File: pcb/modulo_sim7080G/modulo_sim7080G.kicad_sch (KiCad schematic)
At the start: 9 parts, among them J1 Conn_01x02, J2 Conn_01x02, J3 Conn_01x07, U1 SIM7080G, U2 TXB0108DQSR

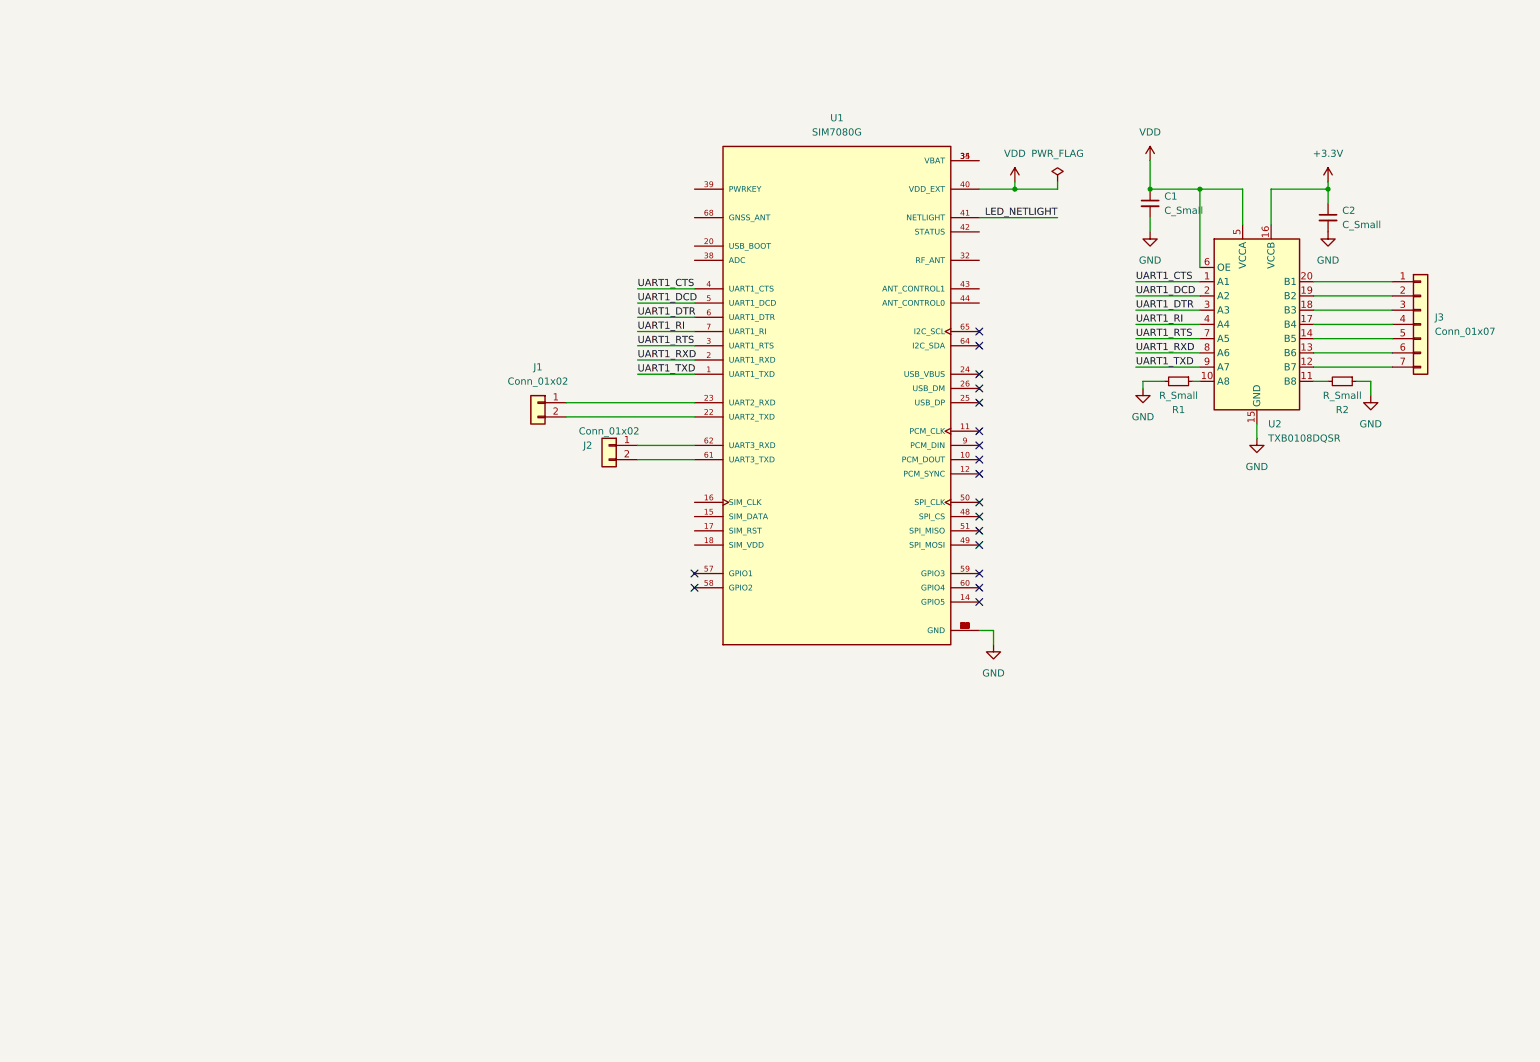
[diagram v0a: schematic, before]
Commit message: update schematic
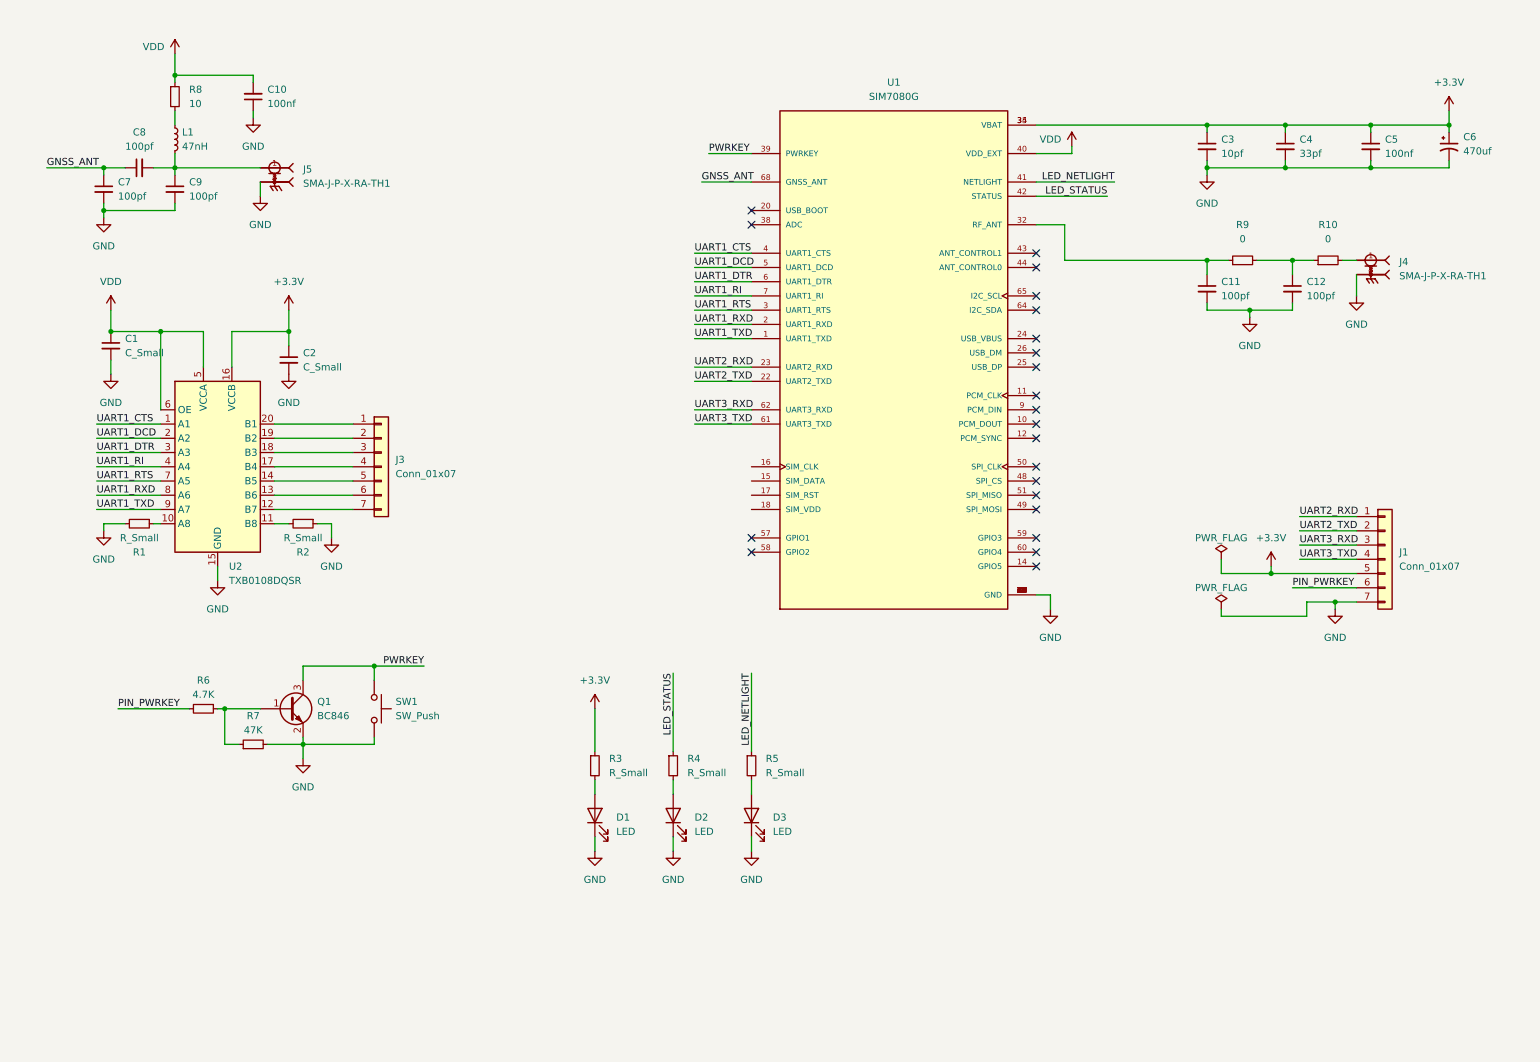
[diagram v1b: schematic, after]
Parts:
- removed J1, J2: Conn_01x02, Connector_PinHeader_2.54mm:PinHeader_1x02_P2.54mm_Vertical, symbol Connector_Generic:Conn_01x02
- added C10, C5: 100nf, Capacitor_SMD:C_0805_2012Metric, symbol Device:C_Small
- added C11, C12, C7, C8, C9: 100pf, Capacitor_SMD:C_0805_2012Metric, symbol Device:C_Small
- added C3: 10pf, Capacitor_SMD:C_0805_2012Metric, symbol Device:C_Small
- added C4: 33pf, Capacitor_SMD:C_0805_2012Metric, symbol Device:C_Small
- added C6: 470uf, Capacitor_Tantalum_SMD:CP_EIA-2012-12_Kemet-R, symbol Device:C_Polarized_Small_US
- added D1, D2, D3: LED, LED_SMD:LED_0805_2012Metric, symbol Device:LED
- added J1: Conn_01x07, Connector_PinHeader_2.54mm:PinHeader_1x07_P2.54mm_Vertical, symbol Connector_Generic:Conn_01x07
- added J4, J5: SMA-J-P-X-RA-TH1, SMA-J-P-X-RA-TH1:SAMTEC_SMA-J-P-X-RA-TH1, symbol SMA-J-P-X-RA-TH1:SMA-J-P-X-RA-TH1
- added L1: 47nH, Inductor_SMD:L_0805_2012Metric, symbol Device:L_Small
- added Q1: BC846, Package_TO_SOT_SMD:SOT-23, symbol Transistor_BJT:BC846
- added R10, R9: 0, Resistor_SMD:R_0805_2012Metric, symbol Device:R_Small
- added R3, R4, R5: R_Small, Resistor_SMD:R_0805_2012Metric, symbol Device:R_Small
- added R6: 4.7K, Resistor_SMD:R_0805_2012Metric, symbol Device:R_Small
- added R7: 47K, Resistor_SMD:R_0805_2012Metric, symbol Device:R_Small
- added R8: 10, Resistor_SMD:R_0805_2012Metric, symbol Device:R_Small
- added SW1: SW_Push, Button_Switch_SMD:SW_SPST_B3U-1000P-B, symbol Switch:SW_Push
- C1, C2: footprint (none) -> Capacitor_SMD:C_0805_2012Metric
- R1, R2: footprint (none) -> Resistor_SMD:R_0805_2012Metric
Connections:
- net +3.3V: now also U1.34 (VBAT), U1.35 (VBAT), C3.1, C4.1, C5.1, C6.1, J1.5 (Pin_5), R3.1
- net GND: now also C10.1, C11.2, C12.2, C3.2, C4.2, C5.2, C6.2, C7.2, C9.2, D1.1 (K), D2.1 (K), D3.1 (K), J1.7 (Pin_7), J4.2, J4.3, J4.4, J4.5, J5.2, J5.3, J5.4, J5.5, Q1.2 (E), R7.2, SW1.2
- net LED_NETLIGHT: now also R5.1
- net VDD: now also C10.2, R8.1
- net UART2_TXD: now reaches U1.22 (UART2_TXD)
- net UART2_TXD: now also J1.2 (Pin_2)
- net UART2_RXD: now reaches U1.23 (UART2_RXD)
- net UART2_RXD: now also J1.1 (Pin_1)
- net at U1.32 (RF_ANT): now also C11.1, R9.1
- net PWRKEY: now reaches U1.39 (PWRKEY)
- net PWRKEY: now also Q1.3 (C), SW1.1
- net LED_STATUS: now reaches U1.42 (STATUS)
- net LED_STATUS: now also R4.1
- net UART3_TXD: now reaches U1.61 (UART3_TXD)
- net UART3_TXD: now also J1.4 (Pin_4)
- net UART3_RXD: now reaches U1.62 (UART3_RXD)
- net UART3_RXD: now also J1.3 (Pin_3)
- net GNSS_ANT: now reaches U1.68 (GNSS_ANT)
- net GNSS_ANT: now also C7.1, C8.1
- new net: D2.2 (A), R4.2
- new net: Q1.1 (B), R6.1, R7.1
- new net: L1.1, R8.2
- new net: J4.1, R10.2
- new net: C8.2, C9.1, J5.1, L1.2
- new net: D1.2 (A), R3.2
- new net: C12.1, R10.1, R9.2
- new net: D3.2 (A), R5.2
- new net PIN_PWRKEY: J1.6 (Pin_6), R6.2
- no-connect marks 18 -> 22
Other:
- moved on the sheet: C1, C2, J3, R1, R2, U1, U2

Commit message: antes del gitignore
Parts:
- removed C1, C2: C_Small, Capacitor_SMD:C_0805_2012Metric, symbol Device:C_Small
- removed C3: 10pf, Capacitor_SMD:C_0805_2012Metric, symbol Device:C_Small
- removed C4: 33pf, Capacitor_SMD:C_0805_2012Metric, symbol Device:C_Small
- removed C5: 100nf, Capacitor_SMD:C_0805_2012Metric, symbol Device:C_Small
- removed C6: 470uf, Capacitor_Tantalum_SMD:CP_EIA-2012-12_Kemet-R, symbol Device:C_Polarized_Small_US
- removed D1, D2, D3: LED, LED_SMD:LED_0805_2012Metric, symbol Device:LED
- removed J1, J3: Conn_01x07, Connector_PinHeader_2.54mm:PinHeader_1x07_P2.54mm_Vertical, symbol Connector_Generic:Conn_01x07
- removed J5: SMA-J-P-X-RA-TH1, SMA-J-P-X-RA-TH1:SAMTEC_SMA-J-P-X-RA-TH1, symbol SMA-J-P-X-RA-TH1:SMA-J-P-X-RA-TH1
- removed Q1: BC846, Package_TO_SOT_SMD:SOT-23, symbol Transistor_BJT:BC846
- removed R1, R2, R3, R4, R5: R_Small, Resistor_SMD:R_0805_2012Metric, symbol Device:R_Small
- removed R6: 4.7K, Resistor_SMD:R_0805_2012Metric, symbol Device:R_Small
- removed R7: 47K, Resistor_SMD:R_0805_2012Metric, symbol Device:R_Small
- removed SW1: SW_Push, Button_Switch_SMD:SW_SPST_B3U-1000P-B, symbol Switch:SW_Push
- removed U1: SIM7080G, SIM7080G:XCVR_SIM7080G, symbol SIM7080G:SIM7080G
- removed U2: TXB0108DQSR, Package_SON:USON-20_2x4mm_P0.4mm, symbol Logic_LevelTranslator:TXB0108DQSR
- added J3: SMA-J-P-X-RA-TH1, SMA-J-P-X-RA-TH1:SAMTEC_SMA-J-P-X-RA-TH1, symbol SMA-J-P-X-RA-TH1:SMA-J-P-X-RA-TH1
- C10, C11, C12, C7, C8, C9: footprint Capacitor_SMD:C_0805_2012Metric -> Capacitor_SMD:C_0402_1005Metric
- R10, R8, R9: footprint Resistor_SMD:R_0805_2012Metric -> Resistor_SMD:R_0402_1005Metric
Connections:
- net GND: now also J3.2, J3.3, J3.4, J3.5
- net at C8.2, C9.1, L1.2: now also J3.1
- no-connect marks 22 -> 0
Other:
- added sheet level_shifters (level_shifters.kicad_sch)
- added sheet modulo_celular (modulo_celular.kicad_sch)
- added sheet signals_input_output (signals_input_output.kicad_sch)
- note added: "MA_MC4G_rev01"
- moved on the sheet: C10, C11, C12, C7, C8, C9, J4, L1, R10, R8, R9

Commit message: antes del CADLAB
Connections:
- net GND: now also C11.1, R9.1; no longer C12.2
- net at C12.1, R10.1, R9.2: now also C12.2
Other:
- note added: "BE_MC4G_rev01"
- note removed: "MA_MC4G_rev01"
- company: (none) -> Autor: Esp. Ing. Mario Aguilar Montoya
- title: (none) -> MODULO DE COMUNICACION 4G SIM8060G
- moved on the sheet: C10, C11, C12, C7, C8, C9, J3, J4, L1, R10, R8, R9

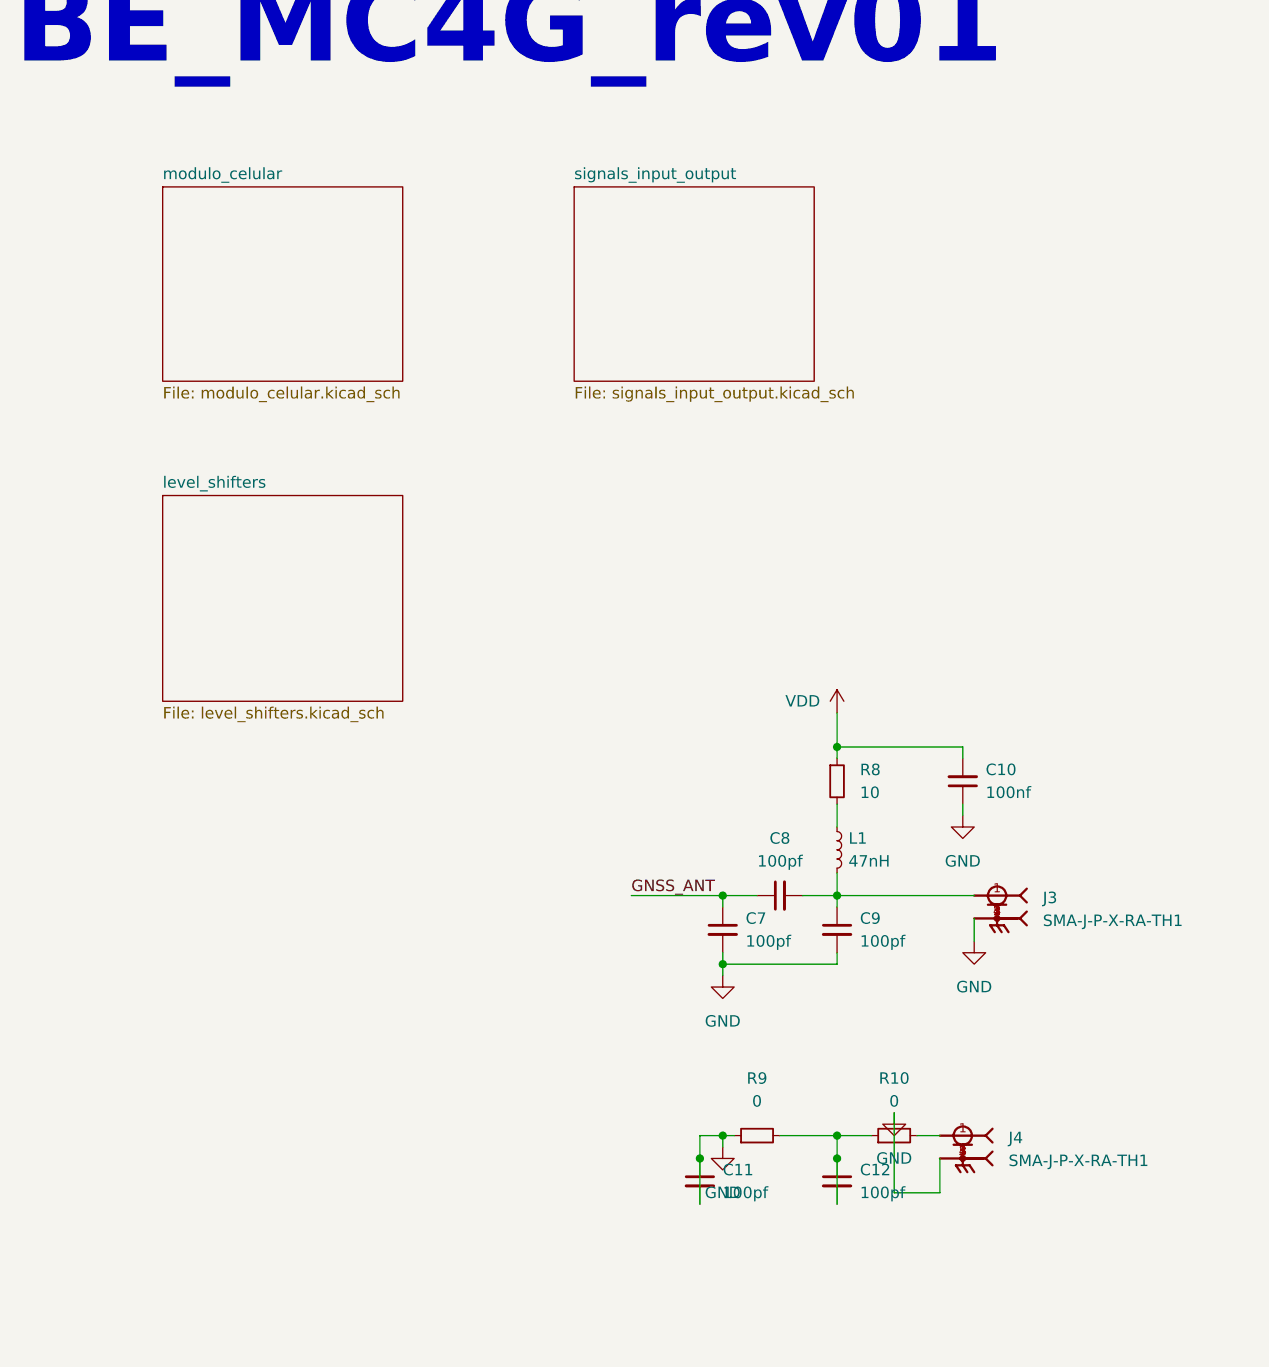
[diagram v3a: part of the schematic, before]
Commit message: se ordenaron los componentes en el pcb
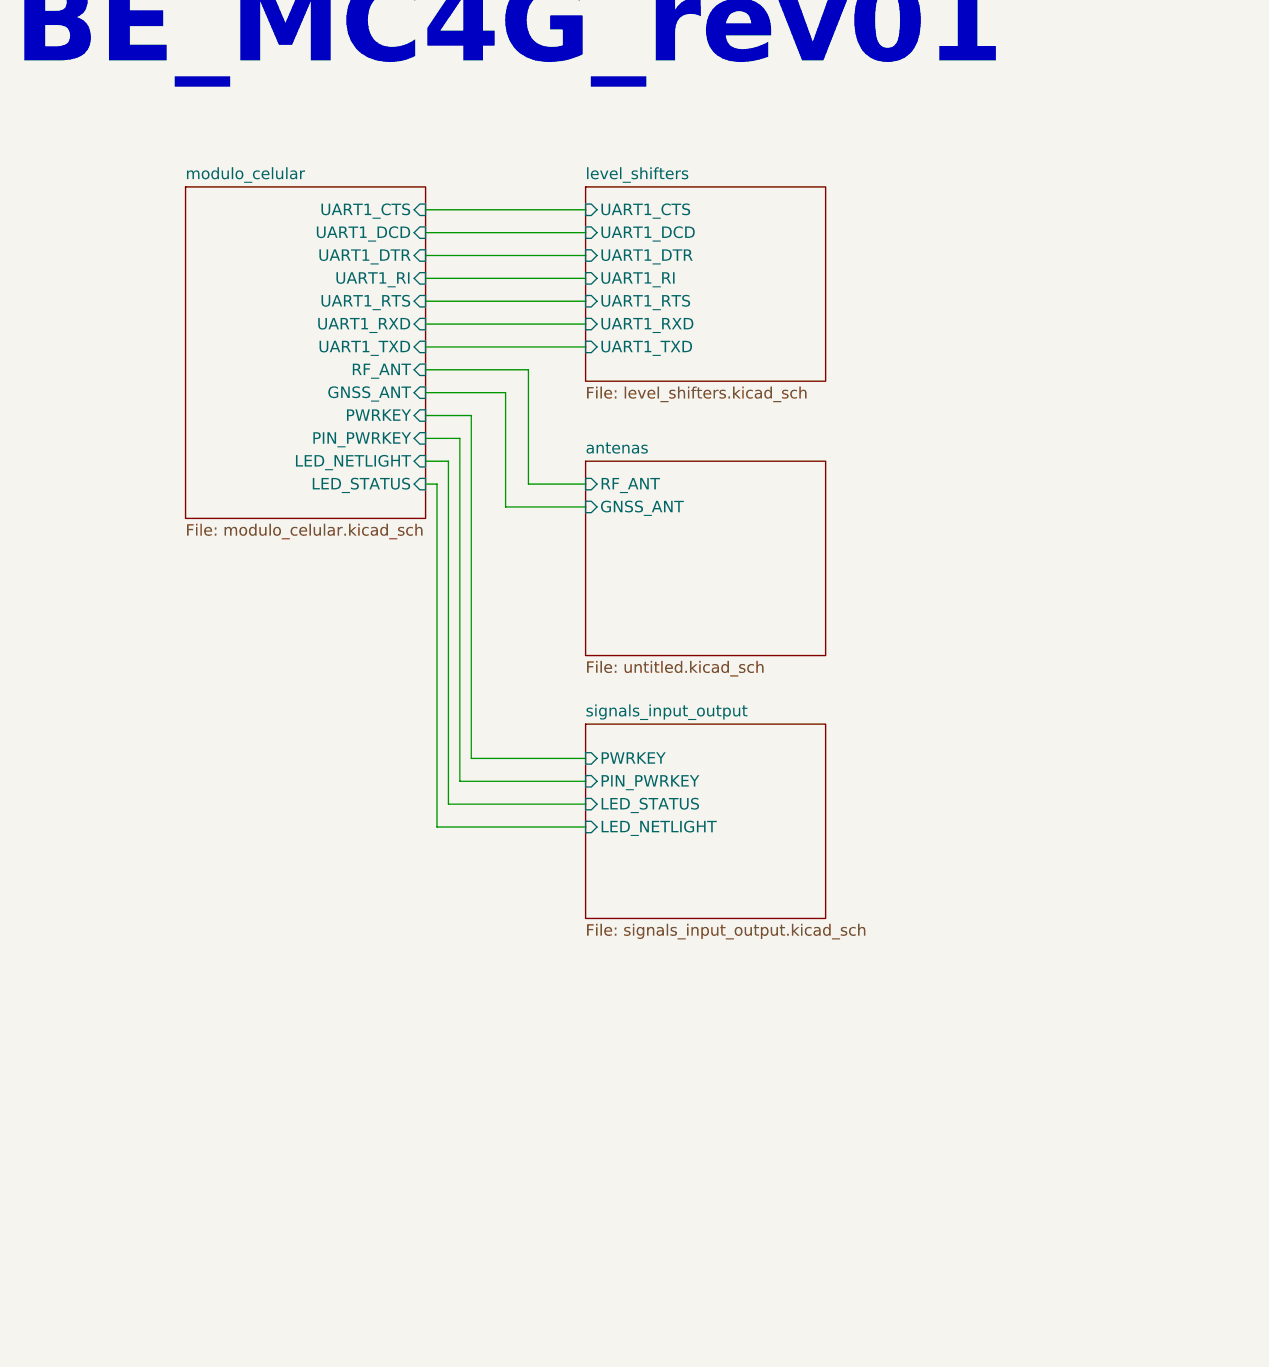
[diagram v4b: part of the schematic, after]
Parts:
- removed C10: 100nf, Capacitor_SMD:C_0402_1005Metric, symbol Device:C_Small
- removed C11, C12, C7, C8, C9: 100pf, Capacitor_SMD:C_0402_1005Metric, symbol Device:C_Small
- removed J3, J4: SMA-J-P-X-RA-TH1, SMA-J-P-X-RA-TH1:SAMTEC_SMA-J-P-X-RA-TH1, symbol SMA-J-P-X-RA-TH1:SMA-J-P-X-RA-TH1
- removed L1: 47nH, Inductor_SMD:L_0805_2012Metric, symbol Device:L_Small
- removed R10, R9: 0, Resistor_SMD:R_0402_1005Metric, symbol Device:R_Small
- removed R8: 10, Resistor_SMD:R_0402_1005Metric, symbol Device:R_Small
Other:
- added sheet antenas (untitled.kicad_sch)
- sheet level_shifters ports: added UART1_CTS, UART1_DCD, UART1_DTR, UART1_RI, UART1_RTS, UART1_RXD, UART1_TXD; removed none
- sheet modulo_celular ports: added GNSS_ANT, LED_NETLIGHT, LED_STATUS, PIN_PWRKEY, PWRKEY, RF_ANT, UART1_CTS, UART1_DCD, UART1_DTR, UART1_RI, UART1_RTS, UART1_RXD, UART1_TXD; removed none
- sheet signals_input_output ports: added LED_NETLIGHT, LED_STATUS, PIN_PWRKEY, PWRKEY; removed none
